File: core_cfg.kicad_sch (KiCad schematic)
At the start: 17 parts, among them U1 NX1H35 PBGA625

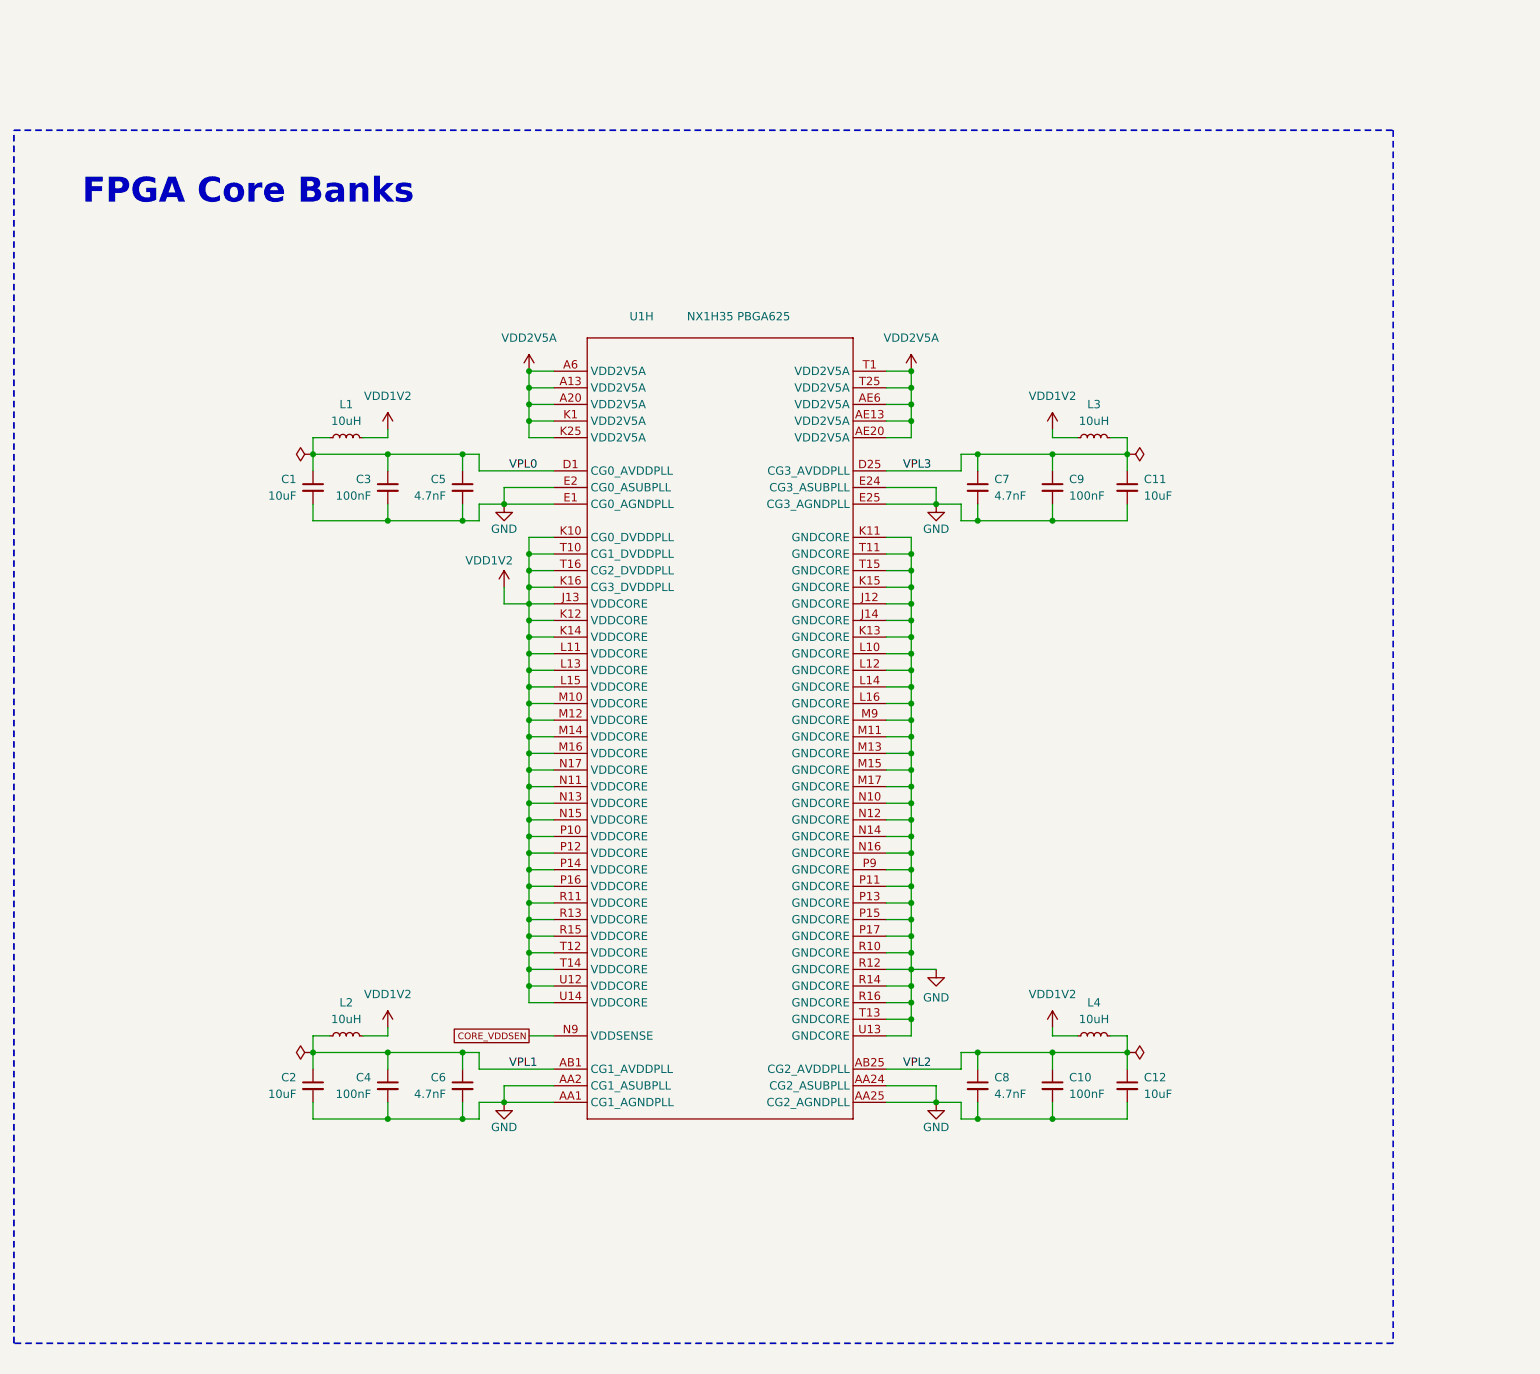
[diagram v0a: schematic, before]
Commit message: pre order checks
ADDED jumper for VDDSENSE remote sensing / 1V2 core PWR for MAX LDO feedback
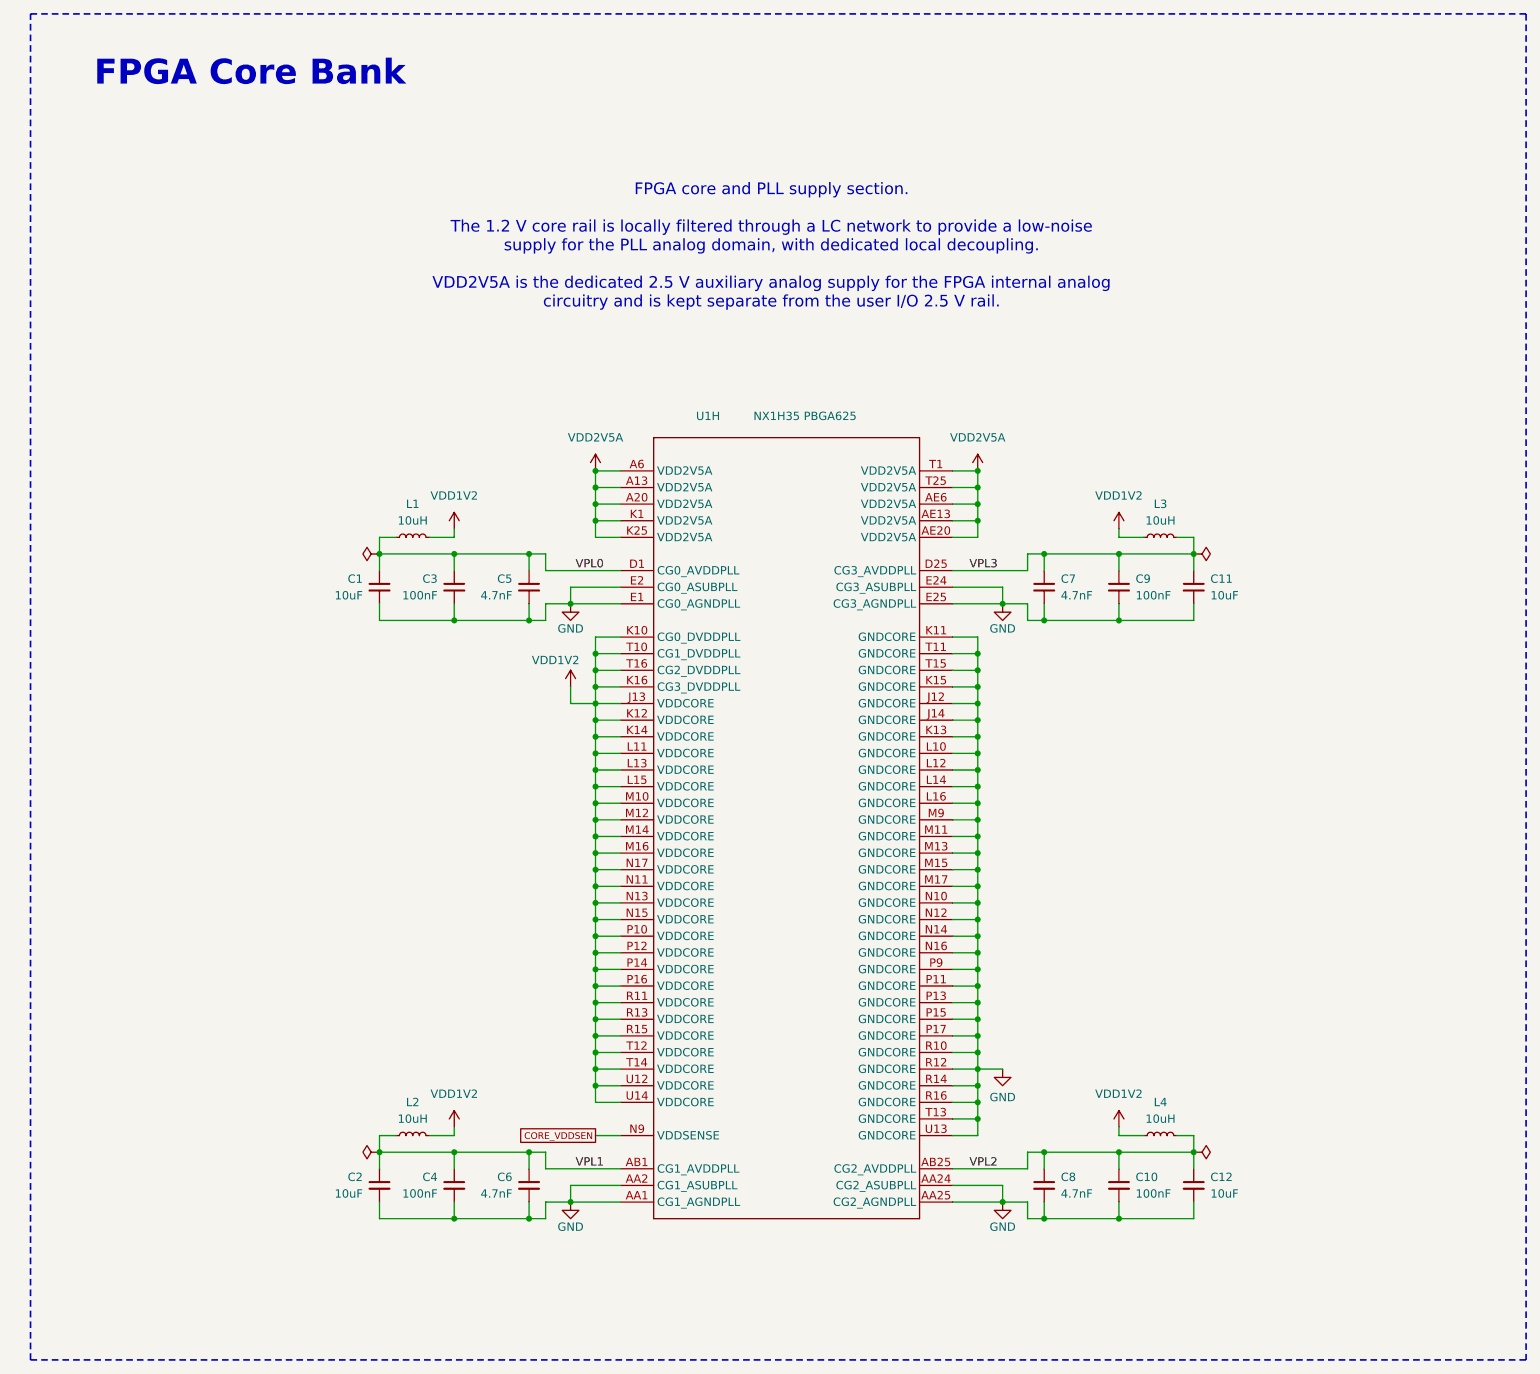
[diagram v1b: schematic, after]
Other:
- note added: "FPGA Core Bank"
- note added: "FPGA core and PLL supply section. The 1.2 V core rail is locally filtered through a LC network to provide a low-noise supply for the PLL analog domain, with dedicated local decoupling. VDD2V5A is the dedicated 2.5 V auxiliary analog supply for the FPGA internal analog circuitry and is kept separate from the user I/O 2.5 V rail."
- note removed: "FPGA Core Banks"
- moved on the sheet: C1, C10, C11, C12, C2, C3, C4, C5, C6, C7, C8, C9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
